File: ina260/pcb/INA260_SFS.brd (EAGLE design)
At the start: 85 x 56 mm, 52 parts

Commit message: finshed first design. after review ready for order
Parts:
- moved U$1 3.00 mm to (27.5, 13.0)
- moved U$6 3.00 mm to (33.7, 13.3)
- moved C_INA1 2.81 mm to (25.9, 7.20)
- moved U$38 2.11 mm to (18.2, 15.1)
- moved U$39 2.11 mm to (23.2, 10.1)
- moved U$40 2.11 mm to (15.7, 15.1)
- moved U$41 2.11 mm to (15.7, 10.1)
- moved U$42 2.11 mm to (20.7, 15.1)
- moved U$43 2.11 mm to (20.7, 10.1)
- moved U$44 2.11 mm to (23.2, 15.1)
- moved U$45 2.11 mm to (18.2, 10.1)
- moved PI1 1.81 mm to (40.0, 4.00)
- moved C_INA3 0.61 mm to (54.9, 47.3)
- moved 5V 0.45 mm to (77.9, 36.8)
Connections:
- net SCL: now also BUS.P$1; no longer BUS.P$2
- net SDA: now also BUS.P$2; no longer BUS.P$1
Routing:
- net SCL: track 31.5 -> 211.1 mm, vias 0 -> 11
- net SDA: track 62.3 -> 185.0 mm, vias 0 -> 11
- net +5V: track 125.7 -> 229.3 mm
- net IN+: track 179.9 -> 199.9 mm
- net GND: track 0.00 -> 5.57 mm, vias 0 -> 42
- net IN-_1: track 5.75 -> 10.2 mm
- net IN-_4: track 11.8 -> 13.2 mm
- net IN-_3: track 8.29 -> 9.59 mm
- net A1_INA3: track 41.4 -> 42.3 mm
- net A1_INA1: track 40.4 -> 41.2 mm
- added copper zone on layer 1, net GND
- added copper zone on layer 16, net GND
- added copper zone on layer 1, net IN+

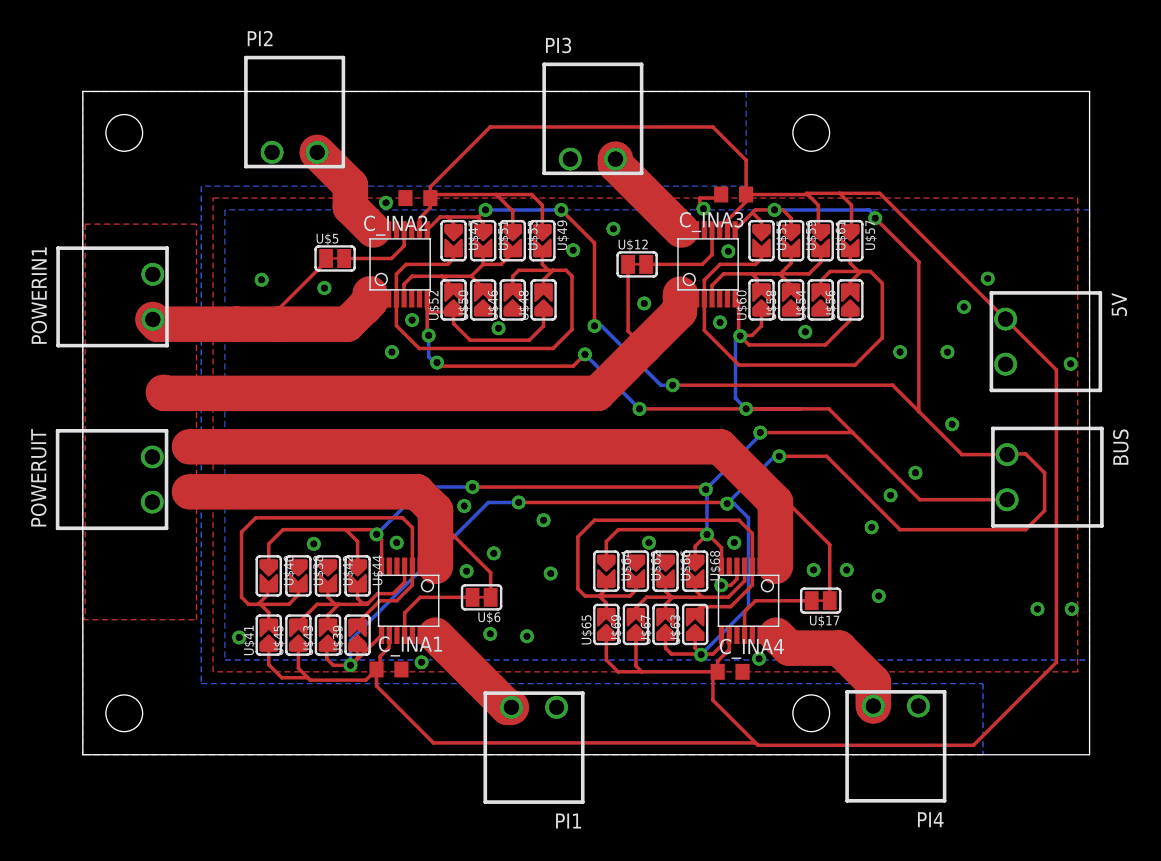
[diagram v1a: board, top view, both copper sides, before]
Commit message: added silkscreen layer pcb
logos added and descriptions of terminals 
also added i2c pullups and alive LED
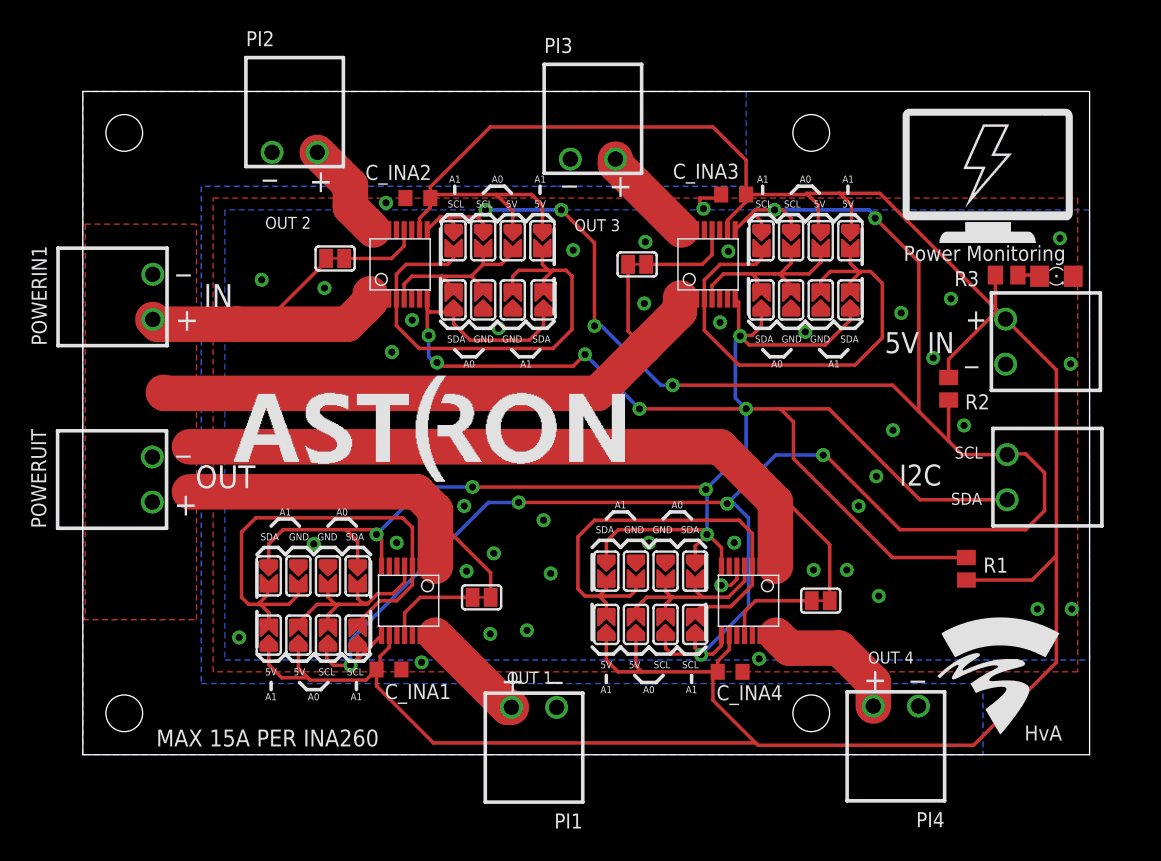
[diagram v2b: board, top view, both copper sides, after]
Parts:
- added 5V_ALIVE_LED: (no value), led:1206
- added R1, R2: 4K7, rcl:M0805
- added R3: 1K, rcl:M0805
- added U$10: (no value), logos:HVA_LOGO
- added U$13: (no value), logos:ASTRON_LOGO
- added U$2: (no value), logos:POWER_MONITORING_LOGO
- added U$3, U$7, U$8, U$9: (no value), logos:JUMPER_INFO
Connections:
- new net N$2: 5V_ALIVE_LED.A, R3.1
- net +5V: now also R1.2, R2.2, R3.2
- net GND: now also 5V_ALIVE_LED.C
- net SCL: now also R2.1
- net SDA: now also R1.1
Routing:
- net +5V: track 229.3 -> 249.2 mm
- net SDA: track 185.0 -> 196.8 mm, vias 11 -> 10
- net SCL: track 211.1 -> 214.7 mm
- net N$2: track 0.00 -> 1.87 mm
- net IN+: track 199.9 -> 198.6 mm
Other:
- board text added: "+"
- board text added: "5V IN"
- board text added: "HvA"
- board text added: "I2C"
- board text added: "IN"
- board text added: "MAX 15A PER INA260"
- board text added: "Made by: Maurizio Giannattasio Bram de Wit Stefan Schokker"
- board text added: "OUT"
- board text added: "OUT 1"
- board text added: "OUT 2"
- board text added: "OUT 3"
- board text added: "OUT 4"
- board text added: "Power Monitoring"
- board text added: "SCL"
- board text added: "SDA"
- board text added: "_"

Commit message: 3.3 volt dc/dc converter
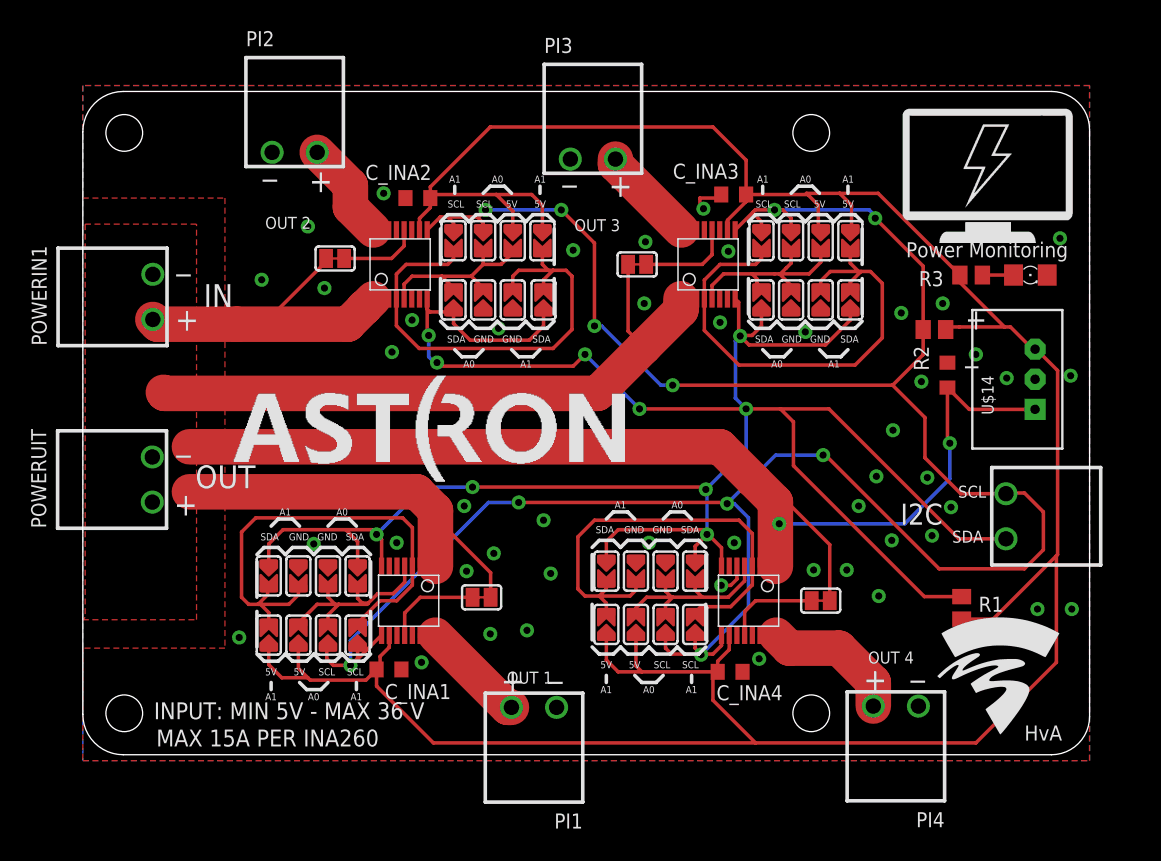
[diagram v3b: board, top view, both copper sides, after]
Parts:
- removed 5V: CON_3.81MM2_SIDE, Phoenix_connector_DJ:CON_3.81MM2
- added C_INA5: 22 uF, Nordic_misc:RESC0805_N
- added U$14: TSR1-2433, Traco power:TSR-1
- moved R2 5.14 mm to (71.9, 35.9), turned to 0 degrees
- moved R1 3.32 mm to (74.2, 12.4)
- moved BUS 3.30 mm to (77.9, 22.0)
- moved R3 3.00 mm to (75.0, 40.5)
- moved 5V_ALIVE_LED 2.20 mm to (80.0, 40.5)
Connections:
- net +5V: now also U$14.3; no longer 5V.P$1
- net GND: now also C_INA5.2, U$14.2; no longer 5V.P$2
- net IN+: now also C_INA5.1, U$14.1
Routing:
- net IN+: track 198.6 -> 232.7 mm, vias 0 -> 2
- net +5V: track 249.2 -> 244.9 mm
- net SDA: track 196.8 -> 199.2 mm
- net N$2: track 1.87 -> 2.63 mm
- net GND: vias 42 -> 48
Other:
- outline, holes or cut-outs redrawn
- board text added: "INPUT: MIN 5V - MAX 36 V"
- board text removed: "5V IN"

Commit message: added I2C second bus line terminal
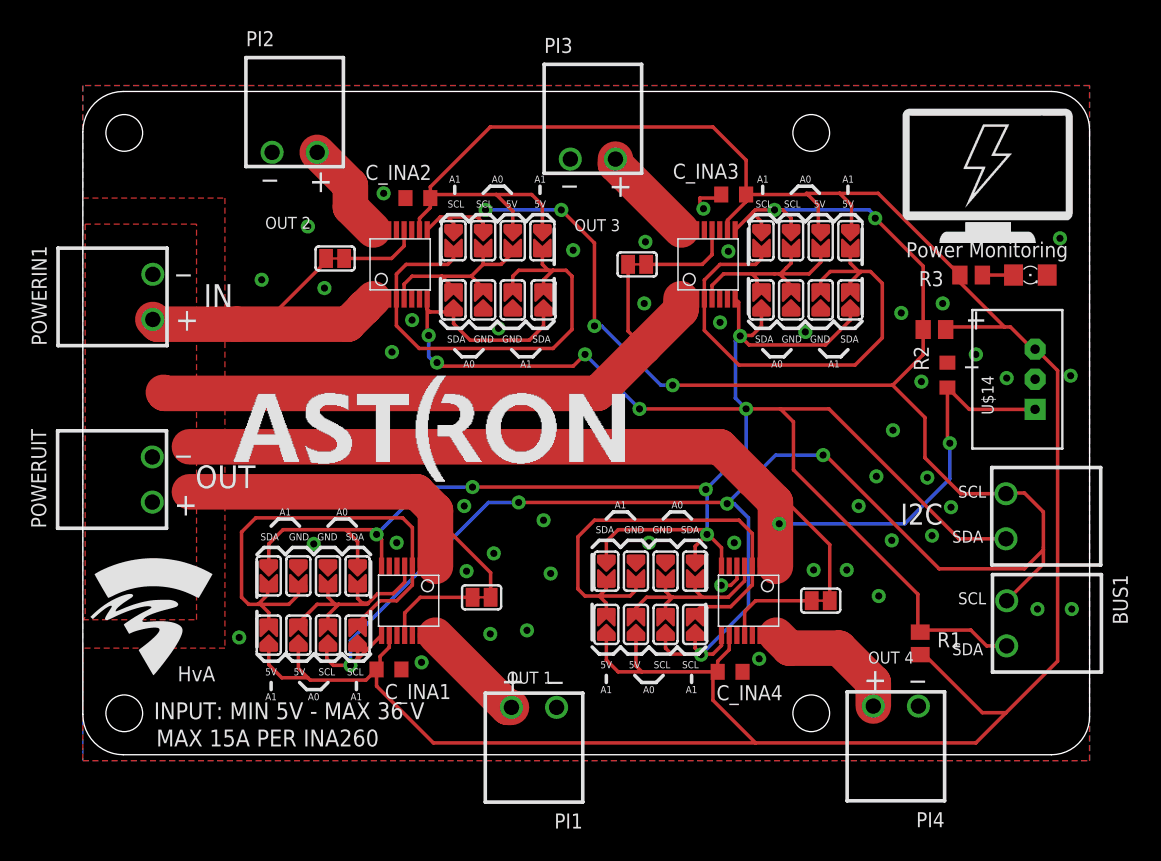
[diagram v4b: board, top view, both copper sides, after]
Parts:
- added BUS1: CON_3.81MM2_SIDE, Phoenix_connector_DJ:CON_3.81MM2
- moved U$10 71.7 mm to (0.00, 5.50)
- moved R1 4.61 mm to (70.7, 9.40)
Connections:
- net SCL: now also BUS1.P$1
- net SDA: now also BUS1.P$2
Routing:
- net SDA: track 199.2 -> 207.1 mm
- net SCL: track 214.7 -> 220.3 mm
- net +5V: track 244.9 -> 243.9 mm
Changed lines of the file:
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@@
 <text x="6.2" y="0.7" size="1.4224" layer="25">MAX 15A PER INA260</text>
 <text x="69.5" y="42" size="1.27" layer="25">Power Monitoring</text>
-<text x="79.5" y="1.2" size="1.27" layer="25">HvA</text>
+<text x="8" y="6.2" size="1.27" layer="25">HvA</text>
 <text x="65.7" y="53.2" size="1.27" layer="26" rot="MR180">Made by:
 Maurizio Giannattasio
@@
 <circle x="3.5" y="52.5" radius="0.5" width="4" layer="42"/>
 <circle x="3.5" y="3.5" radius="0.5" width="4" layer="42"/>
+<text x="73.4" y="8.4" size="1.016" layer="25">SDA</text>
+<text x="73.9" y="12.7" size="1.016" layer="25">SCL</text>
 </plain>
 <attributes>
@@
 <element name="U$68" library="SFS" package="SOLDERJUMPER_ARROW_NOPASTE" value="JUMPER" x="51.7" y="15.5" smashed="yes" rot="R270"/>
 <element name="U$69" library="SFS" package="SOLDERJUMPER_ARROW_NOPASTE" value="JUMPER" x="46.7" y="11" smashed="yes" rot="R90"/>
-<element name="R1" library="rcl" library_urn="urn:adsk.eagle:library:334" package="M0805" package3d_urn="urn:adsk.eagle:package:23556/2" value="4K7" x="74.2" y="12.4" smashed="yes" rot="R270">
-<attribute name="NAME" x="75.63" y="12.07" size="1.27" layer="25"/>
-<attribute name="POPULARITY" value="45" x="74.2" y="12.4" size="1.778" layer="27" rot="R270" display="off"/>
-<attribute name="SPICEPREFIX" value="R" x="74.2" y="12.4" size="1.778" layer="27" rot="R270" display="off"/>
+<element name="R1" library="rcl" library_urn="urn:adsk.eagle:library:334" package="M0805" package3d_urn="urn:adsk.eagle:package:23556/2" value="4K7" x="70.7" y="9.4" smashed="yes" rot="R270">
+<attribute name="NAME" x="72.13" y="9.07" size="1.27" layer="25"/>
+<attribute name="POPULARITY" value="45" x="70.7" y="9.4" size="1.778" layer="27" rot="R270" display="off"/>
+<attribute name="SPICEPREFIX" value="R" x="70.7" y="9.4" size="1.778" layer="27" rot="R270" display="off"/>
 </element>
 <element name="R2" library="rcl" library_urn="urn:adsk.eagle:library:334" package="M0805" package3d_urn="urn:adsk.eagle:package:23556/2" value="4K7" x="71.9" y="35.9" smashed="yes">
@@
 <element name="U$8" library="logos" package="JUMPER_INFO" value="" x="65.8" y="36.6" smashed="yes" rot="R180"/>
 <element name="U$9" library="logos" package="JUMPER_INFO" value="" x="39.8" y="36.6" smashed="yes" rot="R180"/>
-<element name="U$10" library="logos" package="HVA_LOGO" value="" x="71.5" y="0.5" smashed="yes"/>
+<element name="U$10" library="logos" package="HVA_LOGO" value="" x="0" y="5.5" smashed="yes"/>
 <element name="U$13" library="logos" package="ASTRON_LOGO" value="" x="12.7" y="23" smashed="yes"/>
 <element name="5V_ALIVE_LED" library="led" library_urn="urn:adsk.eagle:library:259" package="1206" package3d_urn="urn:adsk.eagle:package:15796/1" value="" x="80" y="40.5" smashed="yes">
@@
 <element name="C_INA5" library="Nordic_misc" package="RESC0805_N" value="22 uF" x="73" y="32.1" smashed="yes" rot="R90">
 <attribute name="VALUE" x="74.9" y="29.5" size="1.27" layer="27" rot="R180"/>
+</element>
+<element name="BUS1" library="Phoenix_connector_DJ" package="CON_3.81MM2" value="CON_3.81MM2_SIDE" x="78" y="13" smashed="yes" rot="R270">
+<attribute name="NAME" x="86.96" y="15.21" size="1.27" layer="25" rot="R270"/>
 </element>
 </elements>
@@
 <wire x1="53.925" y1="15.9" x2="53.925" y2="17.475" width="0.3" layer="1"/>
 <contactref element="R1" pad="1"/>
-<wire x1="71.05" y1="13.35" x2="74.2" y2="13.35" width="0.3" layer="1"/>
-<wire x1="71.05" y1="13.35" x2="60" y2="24.4" width="0.3" layer="1"/>
 <wire x1="52.6" y1="22.4" x2="56" y2="25.8" width="0.3" layer="16"/>
 <wire x1="56" y1="25.8" x2="56" y2="29.2" width="0.3" layer="16"/>
 <wire x1="60" y1="28.1" x2="58.9" y2="29.2" width="0.3" layer="1"/>
-<wire x1="60" y1="24.4" x2="60" y2="28.1" width="0.3" layer="1"/>
+<contactref element="BUS1" pad="P$2"/>
+<wire x1="60" y1="24.05" x2="60" y2="28.1" width="0.3" layer="1"/>
+<wire x1="70.7" y1="10.35" x2="70.525" y2="10.525" width="0.3" layer="1"/>
+<wire x1="78" y1="9.19" x2="76.31" y2="9.19" width="0.3" layer="1"/>
+<wire x1="76.31" y1="9.19" x2="74.975" y2="10.525" width="0.3" layer="1"/>
+<wire x1="70.7" y1="10.35" x2="70.875" y2="10.525" width="0.3" layer="1"/>
+<wire x1="70.875" y1="10.525" x2="74.975" y2="10.525" width="0.3" layer="1"/>
+<wire x1="70.7" y1="10.35" x2="70.5" y2="10.55" width="0.3" layer="1"/>
+<wire x1="70.5" y1="13.55" x2="60" y2="24.05" width="0.3" layer="1"/>
+<wire x1="70.5" y1="10.55" x2="70.5" y2="13.55" width="0.3" layer="1"/>
 </signal>
 <signal name="SCL">
@@
 <wire x1="78" y1="22.1" x2="77.94" y2="22.04" width="0.3" layer="1"/>
 <wire x1="62.7" y1="25.3" x2="72.3" y2="15.7" width="0.3" layer="1"/>
-<wire x1="81.1" y1="17.3" x2="81.1" y2="20.5" width="0.3" layer="1"/>
+<wire x1="81.1" y1="17.3" x2="81.1" y2="17.5" width="0.3" layer="1"/>
+<wire x1="81.1" y1="17.5" x2="81.1" y2="20.5" width="0.3" layer="1"/>
 <wire x1="25.225" y1="10.1" x2="22.675" y2="7.55" width="0.3" layer="1"/>
 <wire x1="22.675" y1="7.55" x2="22.6" y2="7.55" width="0.3" layer="1"/>
@@
 <wire x1="70.95" y1="35.9" x2="70.95" y2="33.78" width="0.3" layer="1"/>
 <wire x1="70.95" y1="33.78" x2="68.37" y2="31.2" width="0.3" layer="1"/>
+<contactref element="BUS1" pad="P$1"/>
+<wire x1="81.1" y1="16.1" x2="81.1" y2="17.3" width="0.3" layer="1"/>
+<wire x1="78" y1="13" x2="81.1" y2="16.1" width="0.3" layer="1"/>
 </signal>
 <signal name="GND">
@@
 <wire x1="53.2" y1="4.6" x2="53.2" y2="7" width="0.3" layer="1"/>
 <wire x1="53.2" y1="7" x2="53.6" y2="7.4" width="0.3" layer="1"/>
-<wire x1="82.3" y1="32.44" x2="82.3" y2="16.9" width="0.3" layer="1"/>
-<wire x1="82.2" y1="16.8" x2="82.2" y2="7.8" width="0.3" layer="1"/>
-<wire x1="82.2" y1="7.8" x2="75.4" y2="1" width="0.3" layer="1"/>
+<wire x1="82.3" y1="32.44" x2="82.3" y2="7.9" width="0.3" layer="1"/>
+<wire x1="82.3" y1="7.9" x2="77.95" y2="3.55" width="0.3" layer="1"/>
+<wire x1="77.95" y1="3.55" x2="75.4" y2="1" width="0.3" layer="1"/>
 <wire x1="75.4" y1="1" x2="56.8" y2="1" width="0.3" layer="1"/>
 <wire x1="56.8" y1="1" x2="29.6" y2="1" width="0.3" layer="1"/>
@@
 <contactref element="R1" pad="2"/>
 <contactref element="R2" pad="2"/>
-<wire x1="74.2" y1="11.45" x2="76.85" y2="11.45" width="0.3" layer="1"/>
-<wire x1="76.85" y1="11.45" x2="82.2" y2="16.8" width="0.3" layer="1"/>
-<wire x1="82.2" y1="16.8" x2="82.3" y2="16.9" width="0.3" layer="1"/>
 <contactref element="R3" pad="2"/>
 <contactref element="U$14" pad="3"/>
@@
 <wire x1="78.31715625" y1="36.11715625" x2="80.1943125" y2="34.24" width="0.3" layer="1"/>
 <wire x1="80.1943125" y1="34.24" x2="80.4" y2="34.24" width="0.3" layer="1"/>
-<wire x1="74" y1="36.11715625" x2="77.81715625" y2="36.11715625" width="0.3" layer="1"/>
+<wire x1="73.06715625" y1="36.11715625" x2="77.81715625" y2="36.11715625" width="0.3" layer="1"/>
 <wire x1="77.81715625" y1="36.11715625" x2="78.31715625" y2="36.11715625" width="0.3" layer="1"/>
 <wire x1="74.05" y1="40.5" x2="67.15" y2="47.4" width="0.3" layer="1"/>
 <wire x1="72.85" y1="35.9" x2="73.06715625" y2="36.11715625" width="0.3" layer="1"/>
-<wire x1="73.06715625" y1="36.11715625" x2="74" y2="36.11715625" width="0.3" layer="1"/>
+<wire x1="77.95" y1="3.55" x2="75.95" y2="3.55" width="0.3" layer="1"/>
+<wire x1="75.95" y1="3.55" x2="71.05" y2="8.45" width="0.3" layer="1"/>
+<wire x1="70.7" y1="8.45" x2="71.05" y2="8.45" width="0.3" layer="1"/>
 </signal>
 <signal name="IN-_1">
